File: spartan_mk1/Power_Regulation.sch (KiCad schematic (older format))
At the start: 33 parts

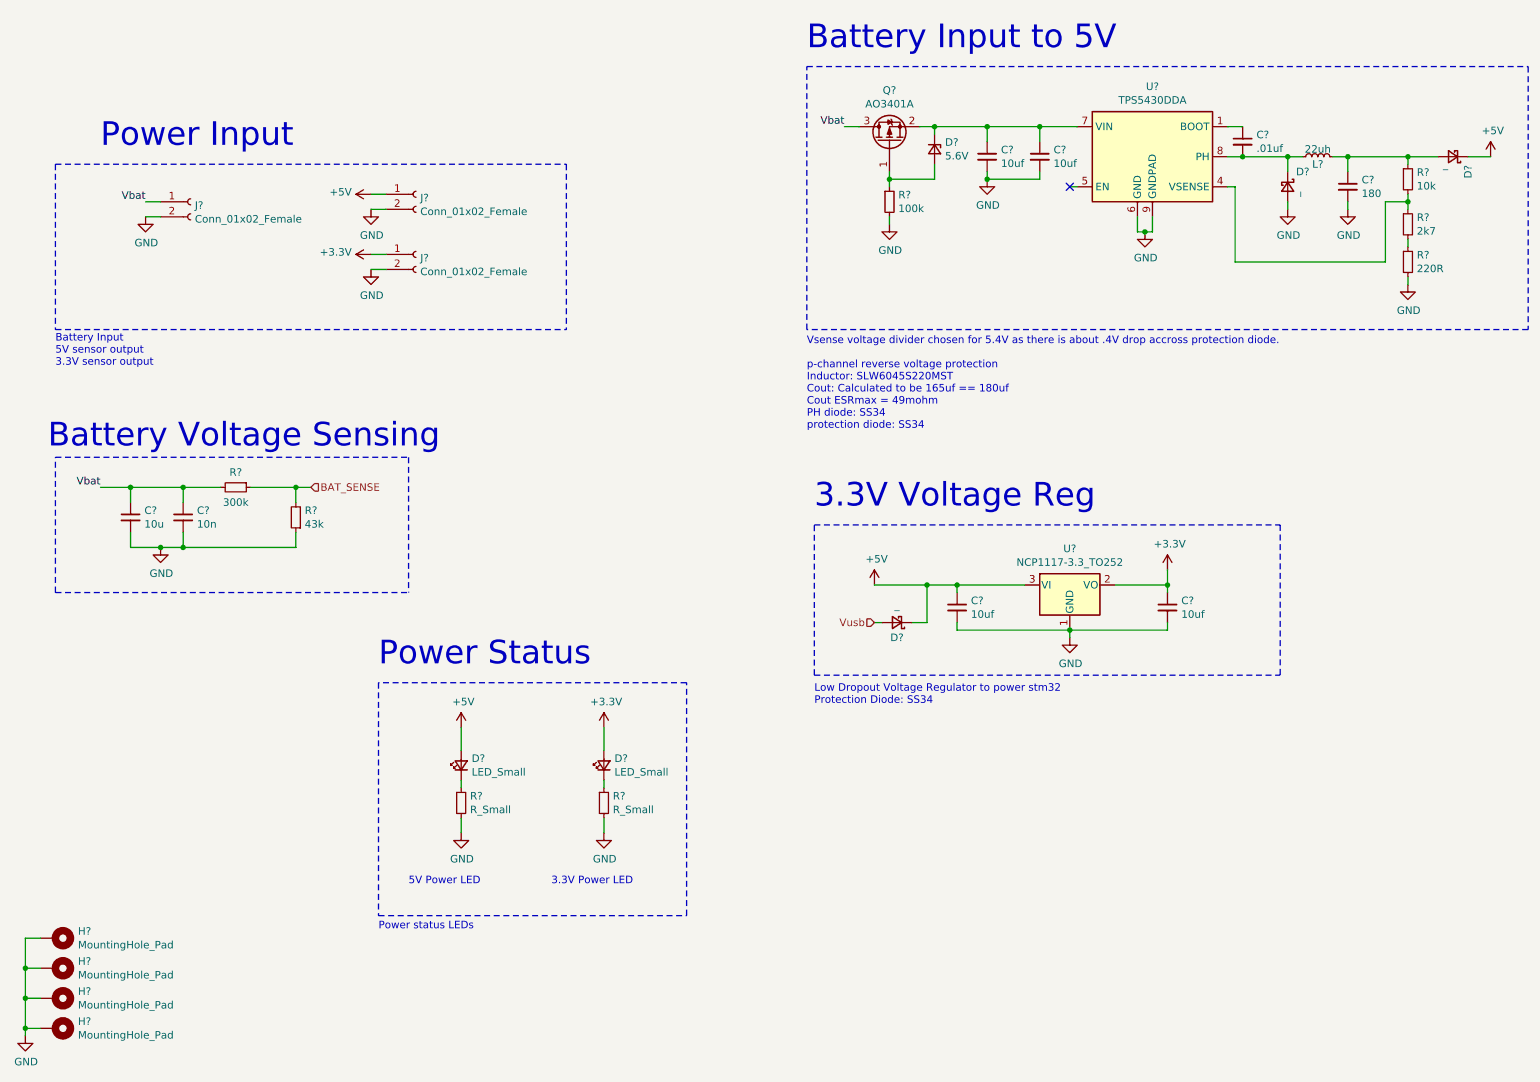
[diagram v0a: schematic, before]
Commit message: Complete schematic with DRC done
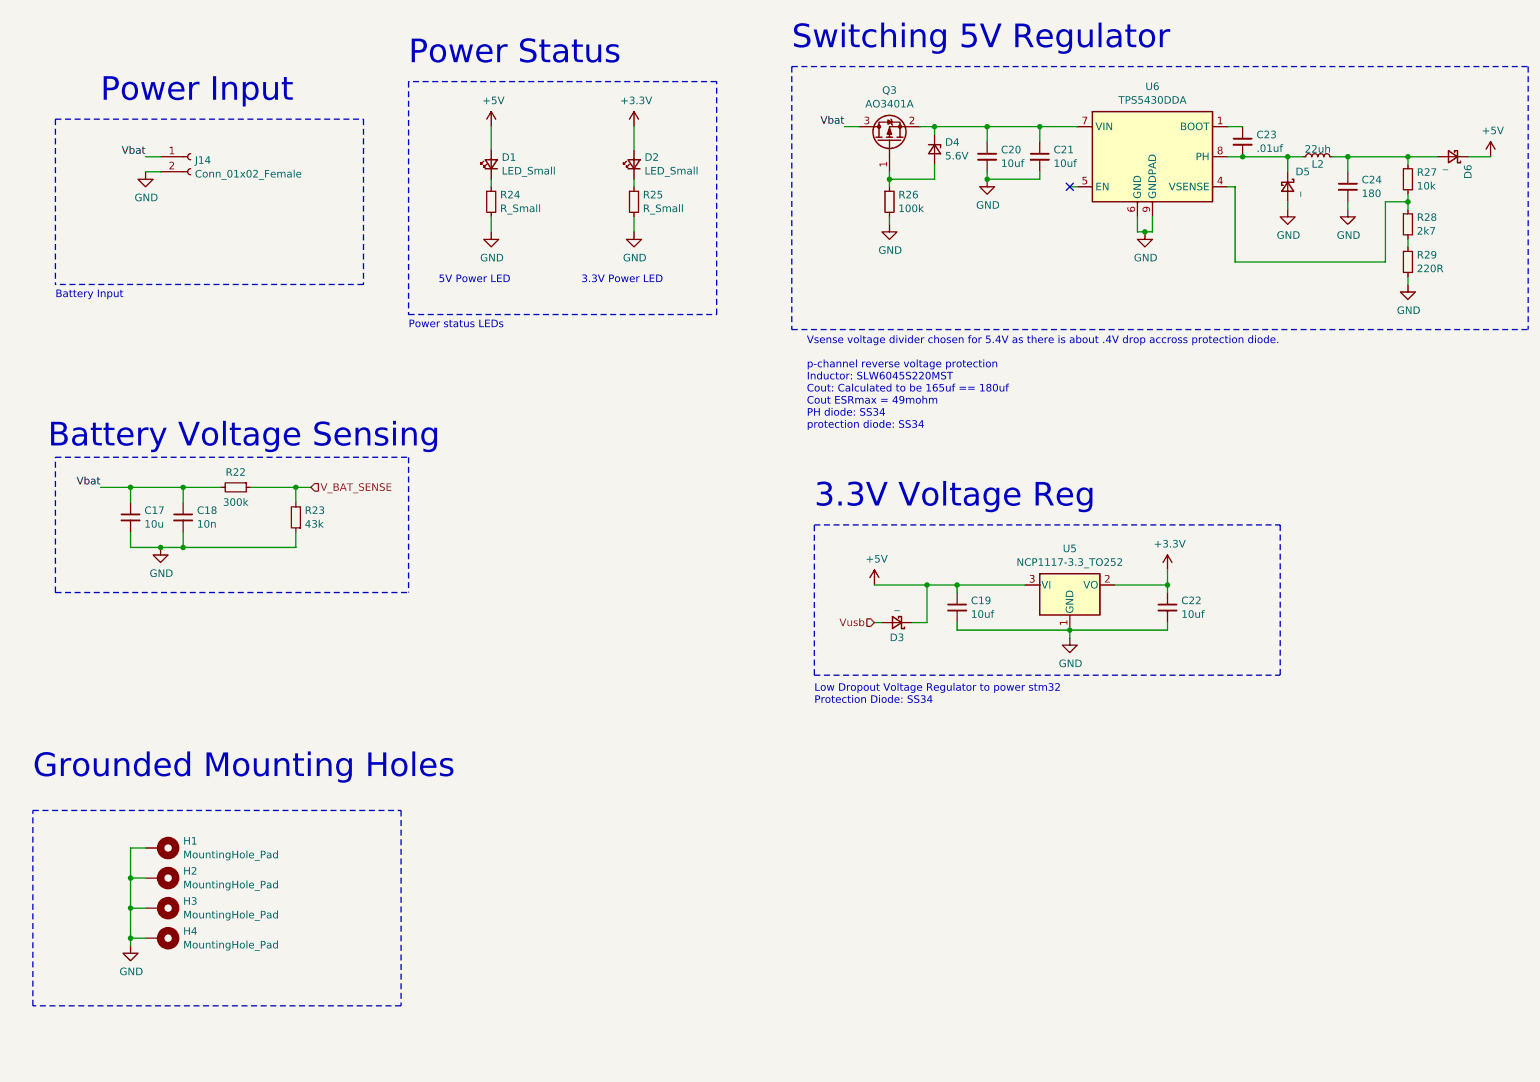
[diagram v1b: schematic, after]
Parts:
- removed J? (x2): Conn_01x02_Female, symbol Connector:Conn_01x02_Female
- gave numbers to parts that had none: 31
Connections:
- net BAT_SENSE renamed V_BAT_SENSE
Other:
- note added: "Battery Input\n"
- note added: "Grounded Mounting Holes"
- note added: "Switching 5V Regulator"
- note removed: "Battery Input to 5V"
- note removed: "Battery Input\n5V sensor output\n3.3V sensor output"
- moved on the sheet: D1, D2, H1, H2, H3, H4, J14, R24, R25

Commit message: Footprints added started PCB placement
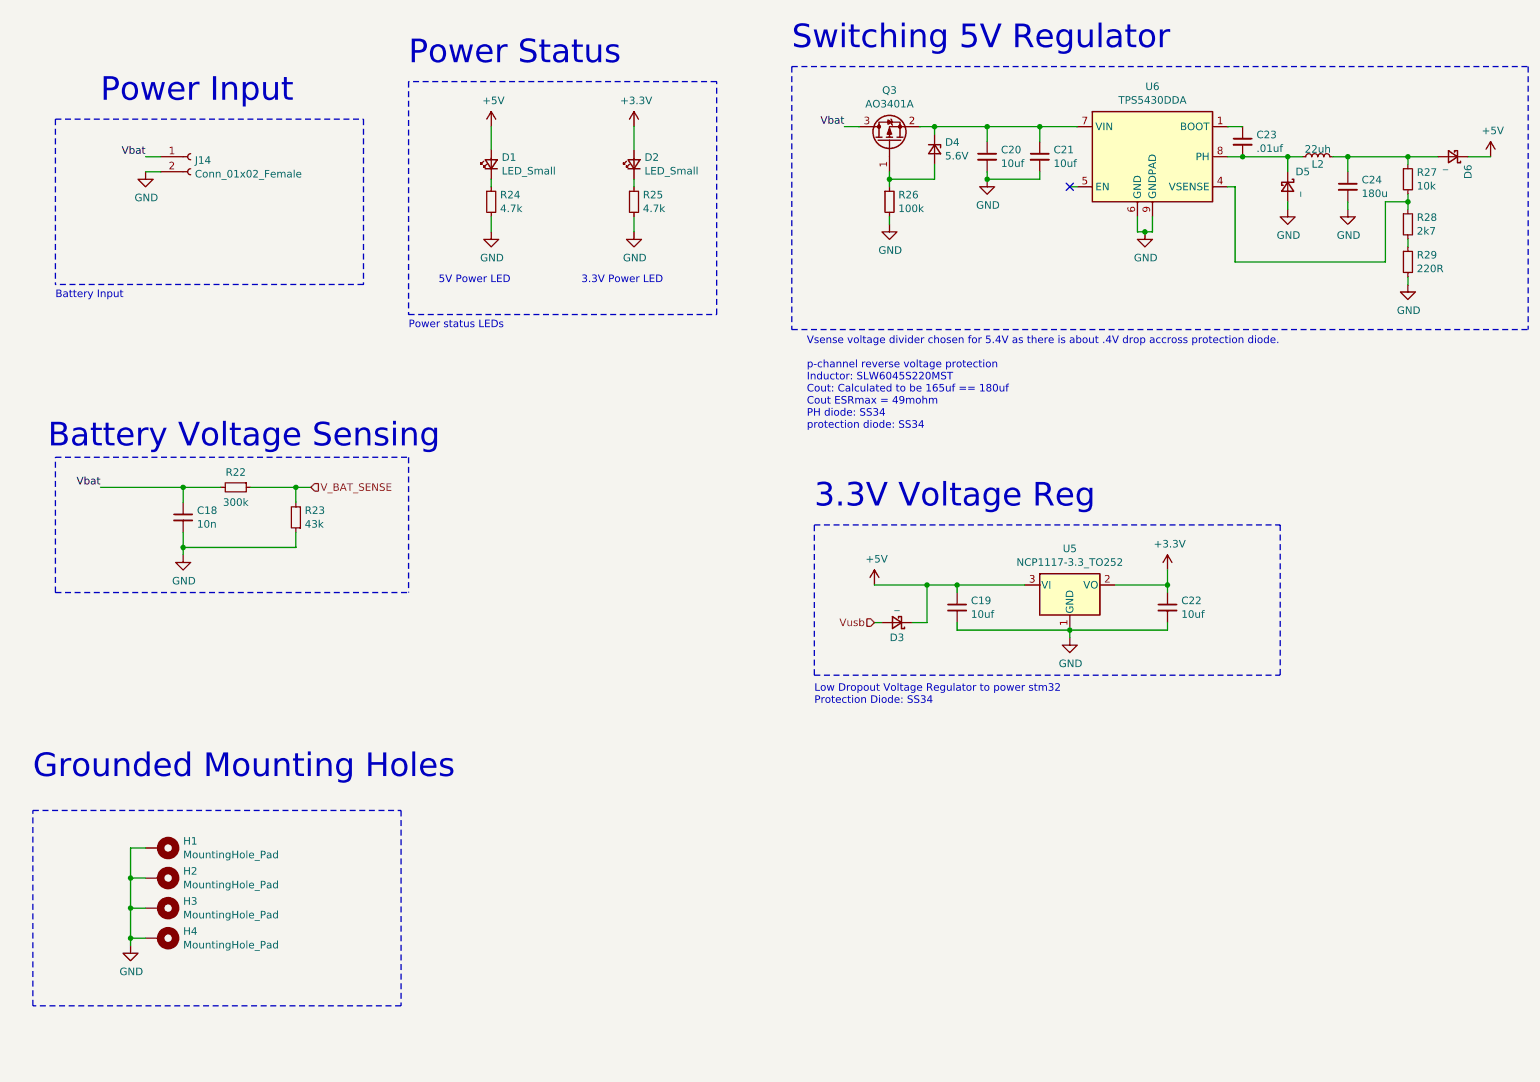
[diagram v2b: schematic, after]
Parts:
- removed C17: 10u, symbol Device:C_Small
- C18, C22: footprint (none) -> Capacitor_SMD:C_0603_1608Metric
- C19: footprint (none) -> Capacitor_SMD:C_0805_2012Metric
- C20, C21: footprint (none) -> Capacitor_SMD:C_1206_3216Metric
- C23: footprint (none) -> Capacitor_SMD:C_0402_1005Metric
- C24: value 180 -> 180u; footprint (none) -> Capacitor_SMD:C_0805_2012Metric_Pad1.15x1.40mm_HandSolder
- D1, D2: footprint (none) -> LED_SMD:LED_0603_1608Metric
- D3, D5, D6: footprint (none) -> Diode_SMD:D_SMA
- D4: footprint (none) -> Diode_SMD:D_MiniMELF
- H1, H2, H3, H4: footprint (none) -> MountingHole:MountingHole_3.2mm_M3_Pad_Via
- J14: footprint (none) -> Connector_SMD:01x02_3mm
- L2: footprint (none) -> Inductor_SMD:SLW6045_6mmX6mm
- R22, R23: footprint (none) -> Resistor_SMD:R_0603_1608Metric
- R24, R25: value R_Small -> 4.7k; footprint (none) -> Resistor_SMD:R_0402_1005Metric
- R26: footprint (none) -> Resistor_SMD:R_0805_2012Metric
- R27, R28, R29: footprint (none) -> Resistor_SMD:R_0402_1005Metric
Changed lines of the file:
@@
 F 0 "J14" H 2028 1526 50  0000 L CNN
 F 1 "Conn_01x02_Female" H 2028 1435 50  0000 L CNN
-F 2 "" H 2000 1550 50  0001 C CNN
+F 2 "Connector_SMD:01x02_3mm" H 2000 1550 50  0001 C CNN
 F 3 "~" H 2000 1550 50  0001 C CNN
 	1    2000 1550
@@
 F 0 "C19" H 7192 4596 50  0000 L CNN
 F 1 "10uf" H 7192 4505 50  0000 L CNN
-F 2 "" H 7100 4550 50  0001 C CNN
+F 2 "Capacitor_SMD:C_0805_2012Metric" H 7100 4550 50  0001 C CNN
 F 3 "~" H 7100 4550 50  0001 C CNN
 	1    7100 4550
@@
 F 0 "C22" H 8592 4596 50  0000 L CNN
 F 1 "10uf" H 8592 4505 50  0000 L CNN
-F 2 "" H 8500 4550 50  0001 C CNN
+F 2 "Capacitor_SMD:C_0603_1608Metric" H 8500 4550 50  0001 C CNN
 F 3 "~" H 8500 4550 50  0001 C CNN
 	1    8500 4550
@@
 F 0 "D2" V 4996 1530 50  0000 R CNN
 F 1 "LED_Small" V 4905 1530 50  0000 R CNN
-F 2 "" V 4950 1600 50  0001 C CNN
+F 2 "LED_SMD:LED_0603_1608Metric" V 4950 1600 50  0001 C CNN
 F 3 "~" V 4950 1600 50  0001 C CNN
 	1    4950 1600
@@
 AR Path="/5F79A745/5F7A605C" Ref="R25"  Part="1"
 F 0 "R25" H 5009 1896 50  0000 L CNN
-F 1 "R_Small" H 5009 1805 50  0000 L CNN
-F 2 "" H 4950 1850 50  0001 C CNN
+F 1 "4.7k" H 5009 1805 50  0000 L CNN
+F 2 "Resistor_SMD:R_0402_1005Metric" H 4950 1850 50  0001 C CNN
 F 3 "~" H 4950 1850 50  0001 C CNN
 	1    4950 1850
@@
 F 0 "C20" H 7392 1596 50  0000 L CNN
 F 1 "10uf" H 7392 1505 50  0000 L CNN
-F 2 "" H 7300 1550 50  0001 C CNN
+F 2 "Capacitor_SMD:C_1206_3216Metric" H 7300 1550 50  0001 C CNN
 F 3 "~" H 7300 1550 50  0001 C CNN
 	1    7300 1550
@@
 F 0 "C23" H 9092 1496 50  0000 L CNN
 F 1 ".01uf" H 9092 1405 50  0000 L CNN
-F 2 "" H 9000 1450 50  0001 C CNN
+F 2 "Capacitor_SMD:C_0402_1005Metric" H 9000 1450 50  0001 C CNN
 F 3 "~" H 9000 1450 50  0001 C CNN
 	1    9000 1450
@@
 F 0 "D5" V 9200 1850 50  0000 C CNN
 F 1 "_" H 9350 1800 50  0000 C CNN
-F 2 "" V 9300 1750 50  0001 C CNN
+F 2 "Diode_SMD:D_SMA" V 9300 1750 50  0001 C CNN
 F 3 "~" V 9300 1750 50  0001 C CNN
 	1    9300 1750
@@
 F 0 "L2" V 9450 1550 50  0000 C CNN
 F 1 "22uh" V 9550 1550 50  0000 C CNN
-F 2 "" H 9500 1550 50  0001 C CNN
+F 2 "Inductor_SMD:SLW6045_6mmX6mm" H 9500 1550 50  0001 C CNN
 F 3 "~" H 9500 1550 50  0001 C CNN
 	1    9500 1550
@@
 AR Path="/5F79A745/5F86A311" Ref="C24"  Part="1"
 F 0 "C24" H 9792 1796 50  0000 L CNN
-F 1 "180" H 9792 1705 50  0000 L CNN
-F 2 "" H 9700 1750 50  0001 C CNN
+F 1 "180u" H 9792 1705 50  0000 L CNN
+F 2 "Capacitor_SMD:C_0805_2012Metric_Pad1.15x1.40mm_HandSolder" H 9700 1750 50  0001 C CNN
 F 3 "~" H 9700 1750 50  0001 C CNN
 	1    9700 1750
@@
 F 0 "C21" H 7742 1596 50  0000 L CNN
 F 1 "10uf" H 7742 1505 50  0000 L CNN
-F 2 "" H 7650 1550 50  0001 C CNN
+F 2 "Capacitor_SMD:C_1206_3216Metric" H 7650 1550 50  0001 C CNN
 F 3 "~" H 7650 1550 50  0001 C CNN
 	1    7650 1550
@@
 F 0 "R28" H 10159 2046 50  0000 L CNN
 F 1 "2k7" H 10159 1955 50  0000 L CNN
-F 2 "" H 10100 2000 50  0001 C CNN
+F 2 "Resistor_SMD:R_0402_1005Metric" H 10100 2000 50  0001 C CNN
 F 3 "~" H 10100 2000 50  0001 C CNN
 	1    10100 2000
@@
 F 0 "R29" H 10159 2296 50  0000 L CNN
 F 1 "220R" H 10159 2205 50  0000 L CNN
-F 2 "" H 10100 2250 50  0001 C CNN
+F 2 "Resistor_SMD:R_0402_1005Metric" H 10100 2250 50  0001 C CNN
 F 3 "~" H 10100 2250 50  0001 C CNN
 	1    10100 2250
@@
 F 0 "D1" V 4046 1530 50  0000 R CNN
 F 1 "LED_Small" V 3955 1530 50  0000 R CNN
-F 2 "" V 4000 1600 50  0001 C CNN
+F 2 "LED_SMD:LED_0603_1608Metric" V 4000 1600 50  0001 C CNN
 F 3 "~" V 4000 1600 50  0001 C CNN
 	1    4000 1600
@@
 AR Path="/5F79A745/5F8C82AC" Ref="R24"  Part="1"
 F 0 "R24" H 4059 1896 50  0000 L CNN
-F 1 "R_Small" H 4059 1805 50  0000 L CNN
-F 2 "" H 4000 1850 50  0001 C CNN
+F 1 "4.7k" H 4059 1805 50  0000 L CNN
+F 2 "Resistor_SMD:R_0402_1005Metric" H 4000 1850 50  0001 C CNN
 F 3 "~" H 4000 1850 50  0001 C CNN
 	1    4000 1850
@@
 F 0 "R27" H 10159 1746 50  0000 L CNN
 F 1 "10k" H 10159 1655 50  0000 L CNN
-F 2 "" H 10100 1700 50  0001 C CNN
+F 2 "Resistor_SMD:R_0402_1005Metric" H 10100 1700 50  0001 C CNN
 F 3 "~" H 10100 1700 50  0001 C CNN
 	1    10100 1700
@@
 F 0 "D3" H 6700 4750 50  0000 C CNN
 F 1 "_" H 6700 4534 50  0000 C CNN
-F 2 "" V 6700 4650 50  0001 C CNN
+F 2 "Diode_SMD:D_SMA" V 6700 4650 50  0001 C CNN
 F 3 "~" V 6700 4650 50  0001 C CNN
 	1    6700 4650
@@
 F 0 "D4" V 6904 1570 50  0000 L CNN
 F 1 "5.6V" V 6995 1570 50  0000 L CNN
-F 2 "" V 6950 1500 50  0001 C CNN
+F 2 "Diode_SMD:D_MiniMELF" V 6950 1500 50  0001 C CNN
 F 3 "~" V 6950 1500 50  0001 C CNN
 	1    6950 1500
@@
 F 0 "R26" H 6709 1896 50  0000 L CNN
 F 1 "100k" H 6709 1805 50  0000 L CNN
-F 2 "" H 6650 1850 50  0001 C CNN
+F 2 "Resistor_SMD:R_0805_2012Metric" H 6650 1850 50  0001 C CNN
 F 3 "~" H 6650 1850 50  0001 C CNN
 	1    6650 1850
@@
 F 0 "D6" V 10300 1650 50  0000 C CNN
 F 1 "_" H 10450 1600 50  0000 C CNN
-F 2 "" V 10400 1550 50  0001 C CNN
+F 2 "Diode_SMD:D_SMA" V 10400 1550 50  0001 C CNN
 F 3 "~" V 10400 1550 50  0001 C CNN
 	1    10400 1550
@@
 F 0 "H1" V 1754 6300 50  0000 L CNN
 F 1 "MountingHole_Pad" V 1845 6300 50  0000 L CNN
-F 2 "" H 1800 6150 50  0001 C CNN
+F 2 "MountingHole:MountingHole_3.2mm_M3_Pad_Via" H 1800 6150 50  0001 C CNN
 F 3 "~" H 1800 6150 50  0001 C CNN
 	1    1800 6150
@@
 F 0 "H2" V 1754 6500 50  0000 L CNN
 F 1 "MountingHole_Pad" V 1845 6500 50  0000 L CNN
-F 2 "" H 1800 6350 50  0001 C CNN
+F 2 "MountingHole:MountingHole_3.2mm_M3_Pad_Via" H 1800 6350 50  0001 C CNN
 F 3 "~" H 1800 6350 50  0001 C CNN
 	1    1800 6350
@@
 F 0 "H3" V 1754 6700 50  0000 L CNN
 F 1 "MountingHole_Pad" V 1845 6700 50  0000 L CNN
-F 2 "" H 1800 6550 50  0001 C CNN
+F 2 "MountingHole:MountingHole_3.2mm_M3_Pad_Via" H 1800 6550 50  0001 C CNN
 F 3 "~" H 1800 6550 50  0001 C CNN
 	1    1800 6550
@@
 F 0 "H4" V 1754 6900 50  0000 L CNN
 F 1 "MountingHole_Pad" V 1845 6900 50  0000 L CNN
-F 2 "" H 1800 6750 50  0001 C CNN
+F 2 "MountingHole:MountingHole_3.2mm_M3_Pad_Via" H 1800 6750 50  0001 C CNN
 F 3 "~" H 1800 6750 50  0001 C CNN
 	1    1800 6750
@@
 F 0 "R23" H 2641 3904 50  0000 R CNN
 F 1 "43k" H 2641 3995 50  0000 R CNN
-F 2 "" H 2700 3950 50  0001 C CNN
+F 2 "Resistor_SMD:R_0603_1608Metric" H 2700 3950 50  0001 C CNN
 F 3 "~" H 2700 3950 50  0001 C CNN
 	1    2700 3950
@@
 F 0 "R22" V 2200 3750 50  0000 C CNN
 F 1 "300k" V 2400 3750 50  0000 C CNN
-F 2 "" H 2300 3750 50  0001 C CNN
+F 2 "Resistor_SMD:R_0603_1608Metric" H 2300 3750 50  0001 C CNN
 F 3 "~" H 2300 3750 50  0001 C CNN
 	1    2300 3750
@@
 $EndComp
 Wire Wire Line
-	1600 4150 1600 4050
-Wire Wire Line
 	1950 4150 2700 4150
-Connection ~ 1950 4150
 Wire Wire Line
 	1950 4150 1950 4050
-Wire Wire Line
-	1800 4150 1600 4150
-Wire Wire Line
-	1800 4150 1950 4150
-Connection ~ 1800 4150
 $Comp
 L power:GND #PWR?
 U 1 1 5F92F707
-P 1800 4150
+P 1950 4200
 AR Path="/5F78701C/5F92F707" Ref="#PWR?"  Part="1"
 AR Path="/5F79A745/5F92F707" Ref="#PWR051"  Part="1"
-F 0 "#PWR051" H 1800 3900 50  0001 C CNN
-F 1 "GND" H 1805 3977 50  0000 C CNN
-F 2 "" H 1800 4150 50  0001 C CNN
-F 3 "" H 1800 4150 50  0001 C CNN
-	1    1800 4150
+F 0 "#PWR051" H 1950 3950 50  0001 C CNN
+F 1 "GND" H 1955 4027 50  0000 C CNN
+F 2 "" H 1950 4200 50  0001 C CNN
+F 3 "" H 1950 4200 50  0001 C CNN
+	1    1950 4200
 	1    0    0    -1
 $EndComp
@@
 Wire Wire Line
 	1950 3750 1950 3850
-Wire Wire Line
-	1400 3750 1600 3750
-Wire Wire Line
-	1600 3750 1950 3750
-Connection ~ 1600 3750
-Wire Wire Line
-	1600 3850 1600 3750
 $Comp
 L Device:C_Small C18
@@
 F 0 "C18" H 2042 3996 50  0000 L CNN
 F 1 "10n" H 2042 3905 50  0000 L CNN
-F 2 "" H 1950 3950 50  0001 C CNN
+F 2 "Capacitor_SMD:C_0603_1608Metric" H 1950 3950 50  0001 C CNN
 F 3 "~" H 1950 3950 50  0001 C CNN
 	1    1950 3950
-	1    0    0    -1
-$EndComp
-$Comp
-L Device:C_Small C17
-U 1 1 5F92F71A
-P 1600 3950
-AR Path="/5F79A745/5F92F71A" Ref="C17"  Part="1"
-AR Path="/5F78701C/5F92F71A" Ref="C?"  Part="1"
-F 0 "C17" H 1692 3996 50  0000 L CNN
-F 1 "10u" H 1692 3905 50  0000 L CNN
-F 2 "" H 1600 3950 50  0001 C CNN
-F 3 "~" H 1600 3950 50  0001 C CNN
-	1    1600 3950
 	1    0    0    -1
 $EndComp
@@
 Wire Notes Line
 	950  7200 950  5900
+Wire Wire Line
+	1400 3750 1950 3750
+Wire Wire Line
+	1950 4200 1950 4150
+Connection ~ 1950 4150
 $EndSCHEMATC
